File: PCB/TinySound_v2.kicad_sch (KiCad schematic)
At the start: 32 parts, among them J4 Conn_01x07

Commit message: Added first version of PCB
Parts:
- removed C11: 100n, Capacitor_SMD:C_0402_1005Metric, symbol Device:C
- removed J1: (no value), symbol Connector_Generic:Conn_01x02
- removed J4: Conn_01x07, symbol Connector_Generic:Conn_01x07
- removed U1: (no value), Package_TO_SOT_SMD:SOT-23-5, symbol Regulator_Linear:MIC5504-3.3YM5
- added J1: Conn_01x07, Connector_PinHeader_2.54mm:PinHeader_1x07_P2.54mm_Vertical, symbol Connector_Generic:Conn_01x07
- added R6, R7: 100k, Resistor_SMD:R_0603_1608Metric_Pad0.98x0.95mm_HandSolder, symbol Device:R
- added TP1, TP2, TP3: TestPoint, TestPoint:TestPoint_Pad_D1.0mm, symbol Connector:TestPoint
- added U1: MIC5504-3.3YMT, TinySound:OnSemi_XDFN4-1EP_1.0x1.0mm_EP0.52x0.52mm, symbol TinySound:MIC5504-3.3YMT
- C1: value (none) -> 100n; footprint (none) -> Capacitor_SMD:C_0402_1005Metric
- C4: footprint (none) -> Capacitor_SMD:C_0805_2012Metric
- J2: value (none) -> USB_B_Micro; footprint (none) -> TinySound:USB_Micro-B_Amphenol_10104110_Horizontal
- J3: value (none) -> Conn_01x07; footprint (none) -> Connector_PinHeader_2.54mm:PinHeader_1x07_P2.54mm_Vertical
- R1: value (none) -> 27R; footprint (none) -> Resistor_SMD:R_0402_1005Metric
- R4: value (none) -> 1k
- R5: value (none) -> 10k
- U2: value (none) -> MAX98360AEFB+T
- U3: value (none) -> RP2040
- U4: value (none) -> W25Q128JVS
- Y1: value (none) -> 12M; footprint (none) -> Crystal:Crystal_SMD_3225-4Pin_3.2x2.5mm
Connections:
- net +3V3: now also J3.1 (Pin_1), U1.1 (VOUT); no longer J3.2 (Pin_2)
- net +5V: now also J1.1 (Pin_1), R6.1, U1.4 (VIN); no longer J3.1 (Pin_1)
- net AU_BCLK: now also U3.36 (GPIO24); no longer U3.6 (GPIO4)
- net AU_DIN: now also U3.34 (GPIO22); no longer U3.8 (GPIO6)
- net AU_EN: now also U3.37 (GPIO25)
- net AU_GAIN: now also R6.2, R7.1
- net AU_LRCLK: now also U3.35 (GPIO23); no longer U3.7 (GPIO5)
- net BOOTSEL: now also TP3.1; no longer J3.3 (Pin_3)
- net GND: now also J3.2 (Pin_2), J1.2 (Pin_2), R7.2, U1.2 (GND), U1.5 (EP); no longer J3.7 (Pin_7)
- net GPIO1: now also U3.30 (GPIO19), J1.5 (Pin_5); no longer U3.17 (GPIO14)
- net GPIO2: now also U3.29 (GPIO18), J1.6 (Pin_6); no longer U3.18 (GPIO15)
- net GPIO3: now also U3.40 (GPIO28/ADC2), J1.7 (Pin_7); no longer U3.27 (GPIO16)
- net RUN: now also J3.7 (Pin_7); no longer J3.6 (Pin_6)
- net SWCLK: now also TP2.1; no longer J3.4 (Pin_4)
- net SWDIO: now also TP1.1; no longer J3.5 (Pin_5)
- net UART_RX: now also J3.6 (Pin_6), U3.7 (GPIO5); no longer U3.3 (GPIO1)
- net UART_TX: now also J3.5 (Pin_5), U3.6 (GPIO4); no longer U3.2 (GPIO0)
- net OUTP: now reaches U2.2 (OUTP)
- net OUTP: now also J1.4 (Pin_4)
- net OUTN: now reaches U2.3 (OUTN)
- net OUTN: now also J1.3 (Pin_3)
- net +1V1: now reaches C13.2, C14.2, C15.2, U3.23 (DVDD), U3.45 (VREG_VOUT), U3.50 (DVDD)
- net XIN: now reaches C18.2, U3.20 (XIN)
- net XIN: now also Y1.3; no longer Y1.1
- net at C17.2, R4.2: now also Y1.1; no longer Y1.3
- net QSPI_SD1: now reaches U3.55 (QSPI_SD1), U4.2 (DO(IO1))
- net QSPI_SD2: now reaches U3.54 (QSPI_SD2), U4.3 (IO2)
- net QSPI_SD0: now reaches U3.53 (QSPI_SD0), U4.5 (DI(IO0))
- net QSPI_SD3: now reaches U3.51 (QSPI_SD3), U4.7 (IO3)
- net XOUT: now reaches R4.1, U3.21 (XOUT)
- net GPIO5: now reaches U3.5 (GPIO3)
- net GPIO5: now also J3.3 (Pin_3)
- net GPIO/ADC: no longer names the net of U3.38 (GPIO26/ADC0)
- new net GPIO4: J3.4 (Pin_4), U3.8 (GPIO6)
- no-connect marks 23 -> 21
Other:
- moved on the sheet: C10, C5, C6, C7, C8, C9, J3, Y1

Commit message: Cleared round traces on PCB, added WS2812 in schematic
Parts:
- added D?: WS2812B, LED_SMD:LED_WS2812B-2020_PLCC4_2.0x2.0mm, symbol LED:WS2812B
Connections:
- net +5V: now also U1.3 (EN), D?.1 (VDD)
- net GND: now also D?.3 (VSS)
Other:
- moved on the sheet: C1, C16, C2, J1, J3, R6, R7, TP1, TP2, TP3, U2, U4

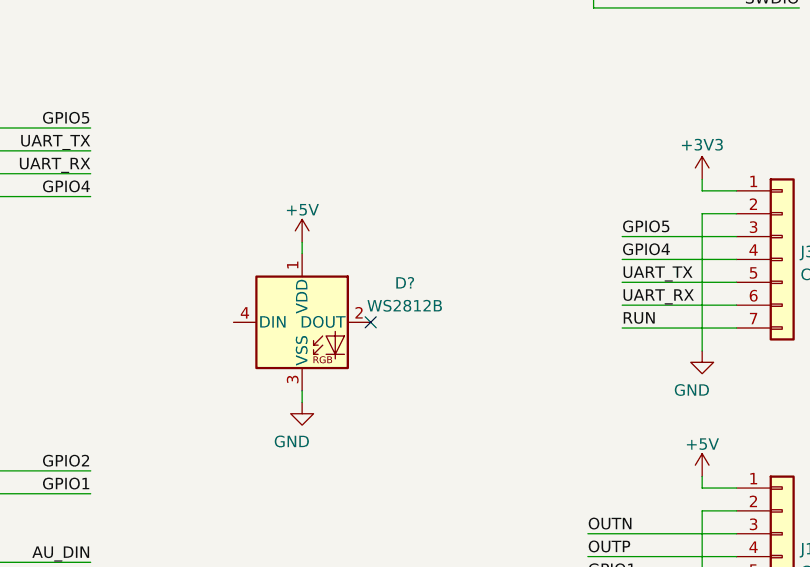
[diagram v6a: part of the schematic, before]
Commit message: New component arrangement vor v2.1
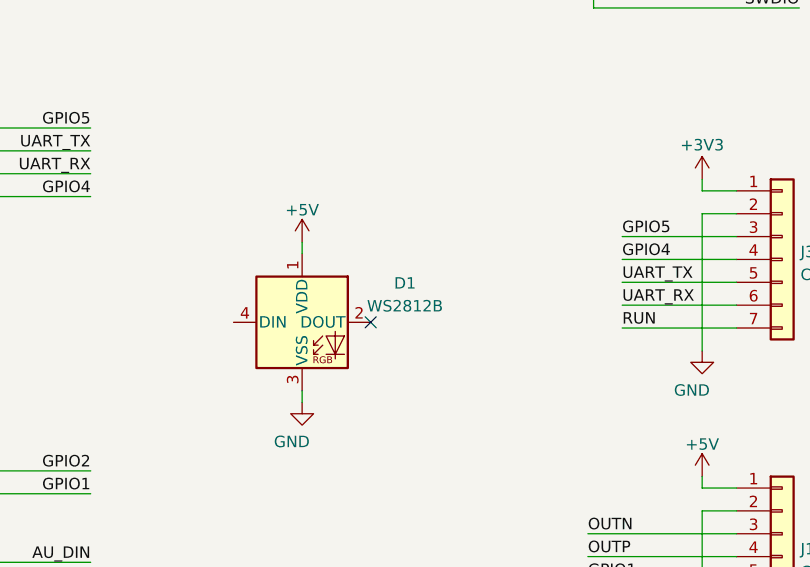
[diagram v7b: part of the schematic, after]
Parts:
- gave numbers to parts that had none: 1
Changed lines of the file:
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@@
   (symbol (lib_id "LED:WS2812B") (at 205.105 116.84 0) (unit 1)
     (in_bom yes) (on_board yes) (fields_autoplaced)
-    (property "Reference" "D?" (id 0) (at 216.535 112.5093 0))
+    (property "Reference" "D1" (id 0) (at 216.535 112.5093 0))
     (property "Value" "WS2812B" (id 1) (at 216.535 115.0493 0))
     (property "Footprint" "LED_SMD:LED_WS2812B-2020_PLCC4_2.0x2.0mm" (id 2) (at 206.375 124.46 0)
@@
   (symbol (lib_id "power:GND") (at 205.105 125.73 0) (unit 1)
     (in_bom yes) (on_board yes)
-    (property "Reference" "#PWR?" (id 0) (at 205.105 132.08 0)
+    (property "Reference" "#PWR022" (id 0) (at 205.105 132.08 0)
       (effects (font (size 1.27 1.27)) hide)
     )
@@
   (symbol (lib_id "power:+5V") (at 205.105 107.95 0) (unit 1)
     (in_bom yes) (on_board yes) (fields_autoplaced)
-    (property "Reference" "#PWR?" (id 0) (at 205.105 111.76 0)
+    (property "Reference" "#PWR012" (id 0) (at 205.105 111.76 0)
       (effects (font (size 1.27 1.27)) hide)
     )
@@
       (reference "#PWR011") (unit 1) (value "GND") (footprint "")
     )
+    (path "/abef0ad7-9284-4bdd-95b2-d8e5d89a9576"
+      (reference "#PWR012") (unit 1) (value "+5V") (footprint "")
+    )
     (path "/c9f2b931-67d5-44ed-9a3e-6c9af7b2b8a8"
       (reference "#PWR013") (unit 1) (value "GND") (footprint "")
@@
       (reference "#PWR021") (unit 1) (value "GND") (footprint "")
     )
+    (path "/543efeb3-c8f5-4846-ae1c-1d9542bbe580"
+      (reference "#PWR022") (unit 1) (value "GND") (footprint "")
+    )
     (path "/da214c8f-94bf-4af2-8be7-334883a47496"
       (reference "#PWR0101") (unit 1) (value "GND") (footprint "")
     )
-    (path "/543efeb3-c8f5-4846-ae1c-1d9542bbe580"
-      (reference "#PWR?") (unit 1) (value "GND") (footprint "")
-    )
-    (path "/abef0ad7-9284-4bdd-95b2-d8e5d89a9576"
-      (reference "#PWR?") (unit 1) (value "+5V") (footprint "")
-    )
     (path "/f916e9cb-a39e-4de7-a5bf-5ef808aada51"
       (reference "C1") (unit 1) (value "100n") (footprint "Capacitor_SMD:C_0402_1005Metric")
@@
     )
     (path "/36b342ba-77cd-4983-af16-96d120dba361"
-      (reference "D?") (unit 1) (value "WS2812B") (footprint "LED_SMD:LED_WS2812B-2020_PLCC4_2.0x2.0mm")
+      (reference "D1") (unit 1) (value "WS2812B") (footprint "LED_SMD:LED_WS2812B-2020_PLCC4_2.0x2.0mm")
     )
     (path "/cf0f3ea6-2132-4e45-b8a4-7fd3c9d79b1a"
